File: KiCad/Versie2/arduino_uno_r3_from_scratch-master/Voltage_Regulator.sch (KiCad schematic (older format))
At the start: 8 parts, among them CON1 BARREL_JACK, U1 LD1117S50TR

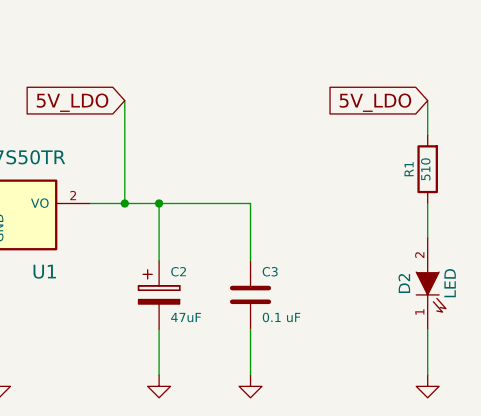
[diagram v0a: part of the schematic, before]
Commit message: 28feb
Aanpassing KiCad+deel footprints
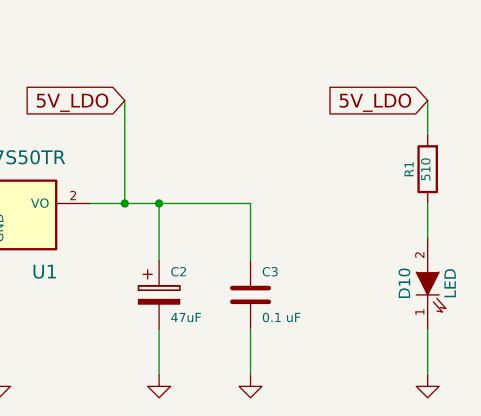
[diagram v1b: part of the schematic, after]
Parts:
- renumbered D2 to D10
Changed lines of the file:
@@
 $EndComp
 $Comp
-L LED-RESCUE-Arduino_Uno_R3_From_Scratch D2
+L LED-RESCUE-Arduino_Uno_R3_From_Scratch D10
 U 1 1 55D1FC7B
 P 7800 4125
-F 0 "D2" H 7800 4225 50  0000 C CNN
+F 0 "D10" H 7800 4225 50  0000 C CNN
 F 1 "LED" H 7800 4025 50  0000 C CNN
 F 2 "~" H 7800 4125 60  0000 C CNN
